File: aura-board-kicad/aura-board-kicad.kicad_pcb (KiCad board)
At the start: 2 copper layers, 76.8 x 53.3 mm, 21 parts, among them J1 Main Power, J2 PWM_3x08, J3 BBCON, J4 Atto, J5 GPS, J6 SBUS, J7 Tele, J8 I2C0, U1 TSR2-2450, U2 PocketBeagle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

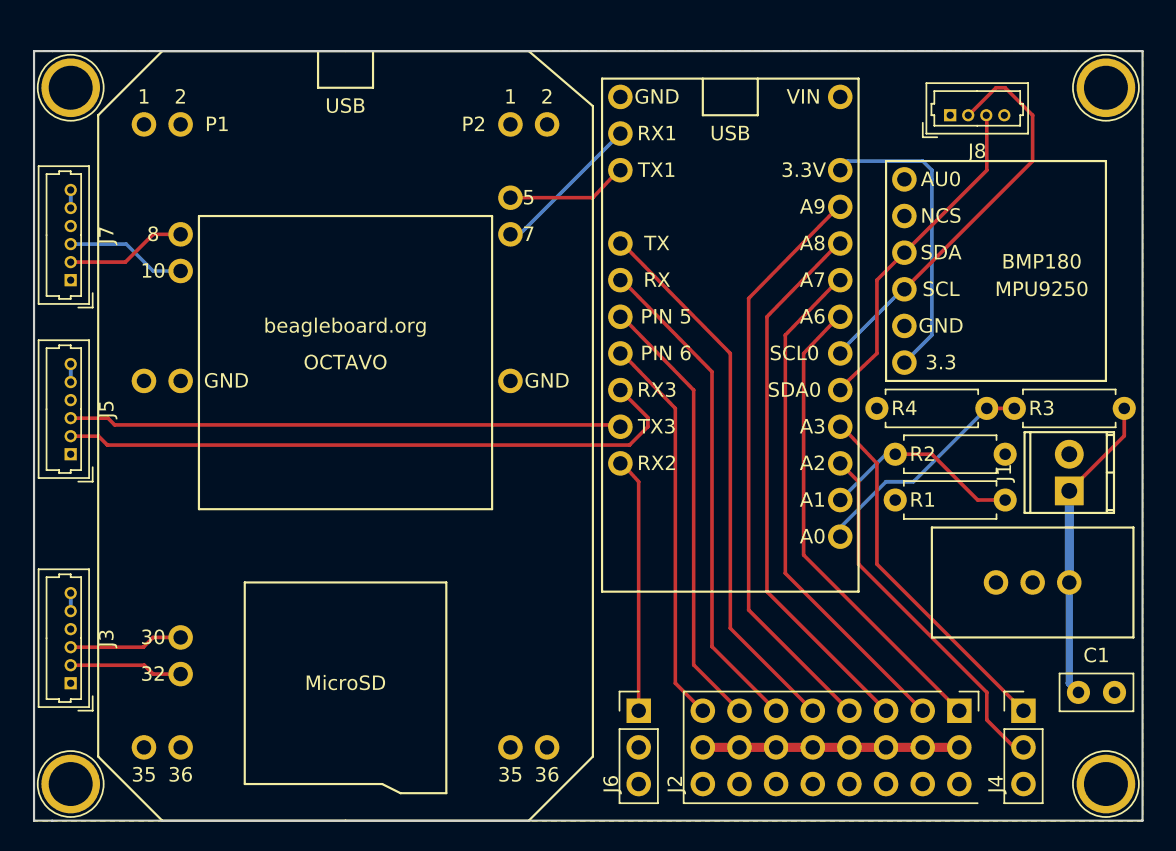
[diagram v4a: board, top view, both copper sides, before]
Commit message: Move some of the F.Fab labels to F.SilkS so they show up on the final board.
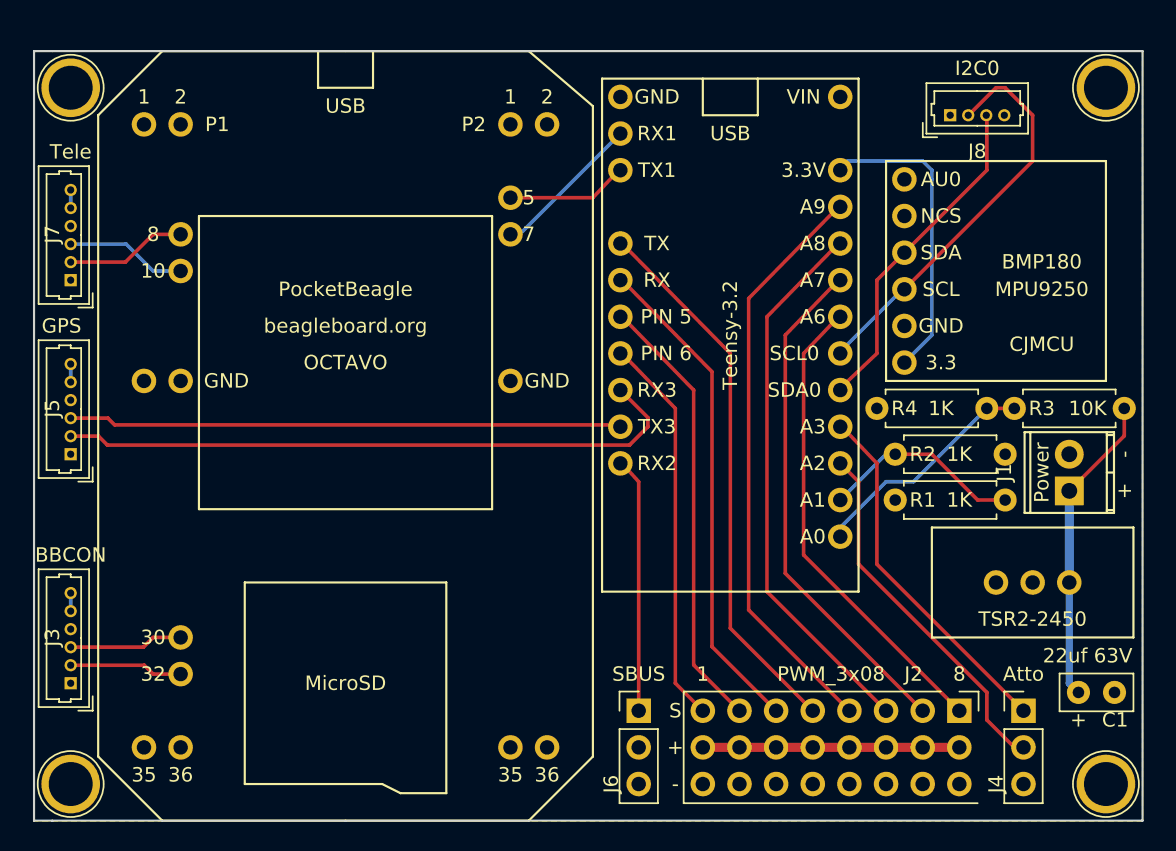
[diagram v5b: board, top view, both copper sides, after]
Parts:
- J1: value Main Power -> Power
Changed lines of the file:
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@@
   (layers
     (0 F.Cu signal hide)
-    (31 B.Cu signal)
+    (31 B.Cu signal hide)
     (32 B.Adhes user)
     (33 F.Adhes user)
@@
   )
   (setup
-    (last_trace_width 0.254)
+    (last_trace_width 0.1524)
     (user_trace_width 0.254)
     (user_trace_width 0.381)
@@
     (visible_elements FFFFFF7F)
     (pcbplotparams
-      (layerselection 0x00030_80000001)
+      (layerselection 0x00020_80000001)
       (usegerberextensions false)
       (excludeedgelayer true)
@@
       (outputformat 1)
       (mirror false)
-      (drillshape 1)
+      (drillshape 0)
       (scaleselection 1)
       (outputdirectory ""))
@@
     (descr "Molex PicoBlade, single row, top entry type, through hole, PN:53047-0610")
     (tags "connector molex picoblade")
-    (fp_text reference J5 (at 3.125 2.5 90) (layer F.SilkS)
-      (effects (font (size 1 1) (thickness 0.15)))
-    )
-    (fp_text value GPS (at 8.89 -0.635 180) (layer F.Fab)
+    (fp_text reference J5 (at 3.175 -1.27 90) (layer F.SilkS)
+      (effects (font (size 1 1) (thickness 0.15)))
+    )
+    (fp_text value GPS (at 8.89 -0.635 180) (layer F.SilkS)
       (effects (font (size 1 1) (thickness 0.15)))
     )
@@
     (fp_line (start -1.9 1.525) (end -1.9 0.525) (layer F.SilkS) (width 0.12))
     (fp_line (start -1.9 1.525) (end -0.9 1.525) (layer F.SilkS) (width 0.12))
-    (fp_text user %R (at 3.125 -1.25 90) (layer F.Fab)
+    (fp_text user %R (at 6.985 2.54 90) (layer F.Fab)
       (effects (font (size 1 1) (thickness 0.15)))
     )
@@
     (descr "Molex PicoBlade, single row, top entry type, through hole, PN:53047-0610")
     (tags "connector molex picoblade")
-    (fp_text reference J3 (at 3.125 2.5 90) (layer F.SilkS)
-      (effects (font (size 1 1) (thickness 0.15)))
-    )
-    (fp_text value BBCON (at 8.89 0 180) (layer F.Fab)
+    (fp_text reference J3 (at 3.175 -1.27 90) (layer F.SilkS)
+      (effects (font (size 1 1) (thickness 0.15)))
+    )
+    (fp_text value BBCON (at 8.89 0 180) (layer F.SilkS)
       (effects (font (size 1 1) (thickness 0.15)))
     )
@@
     (fp_line (start -1.9 1.525) (end -1.9 0.525) (layer F.SilkS) (width 0.12))
     (fp_line (start -1.9 1.525) (end -0.9 1.525) (layer F.SilkS) (width 0.12))
-    (fp_text user %R (at 3.125 -1.25 90) (layer F.Fab)
+    (fp_text user %R (at 6.985 2.54 90) (layer F.Fab)
       (effects (font (size 1 1) (thickness 0.15)))
     )
@@
     (descr "Molex PicoBlade, single row, top entry type, through hole, PN:53047-0610")
     (tags "connector molex picoblade")
-    (fp_text reference J7 (at 3.125 2.5 90) (layer F.SilkS)
-      (effects (font (size 1 1) (thickness 0.15)))
-    )
-    (fp_text value Tele (at 8.89 0 180) (layer F.Fab)
+    (fp_text reference J7 (at 3.175 -1.27 90) (layer F.SilkS)
+      (effects (font (size 1 1) (thickness 0.15)))
+    )
+    (fp_text value Tele (at 8.89 0 180) (layer F.SilkS)
       (effects (font (size 1 1) (thickness 0.15)))
     )
@@
     (fp_line (start -1.9 1.525) (end -1.9 0.525) (layer F.SilkS) (width 0.12))
     (fp_line (start -1.9 1.525) (end -0.9 1.525) (layer F.SilkS) (width 0.12))
-    (fp_text user %R (at 3.125 -1.25 90) (layer F.Fab)
+    (fp_text user %R (at 6.35 2.54 90) (layer F.Fab)
       (effects (font (size 1 1) (thickness 0.15)))
     )
@@
       (effects (font (size 1 1) (thickness 0.15)))
     )
-    (fp_text value I2C0 (at 1.875 -3.25) (layer F.Fab)
+    (fp_text value I2C0 (at 1.875 -3.25) (layer F.SilkS)
       (effects (font (size 1 1) (thickness 0.15)))
     )
@@
     (descr "Through hole straight pin header, 1x08, 2.54mm pitch, single row")
     (tags "Through hole pin header THT 1x08 2.54mm single row")
-    (fp_text reference J2 (at 5.08 19.685 270) (layer F.SilkS)
-      (effects (font (size 1 1) (thickness 0.15)))
-    )
-    (fp_text value PWM_3x08 (at -2.54 8.89 360) (layer F.Fab)
+    (fp_text reference J2 (at -2.54 3.175 360) (layer F.SilkS)
+      (effects (font (size 1 1) (thickness 0.15)))
+    )
+    (fp_text value PWM_3x08 (at -2.54 8.89 360) (layer F.SilkS)
       (effects (font (size 1 1) (thickness 0.15)))
     )
@@
       (effects (font (size 1 1) (thickness 0.15)))
     )
-    (fp_text value 1K (at 3.81 2.31) (layer F.Fab)
+    (fp_text value 1K (at 5.715 3.175) (layer F.SilkS)
       (effects (font (size 1 1) (thickness 0.15)))
     )
@@
       (effects (font (size 1 1) (thickness 0.15)))
     )
-    (fp_text value 10K (at 5.08 0) (layer F.Fab)
+    (fp_text value 10K (at 5.08 0) (layer F.SilkS)
       (effects (font (size 1 1) (thickness 0.15)))
     )
@@
       (effects (font (size 1 1) (thickness 0.15)))
     )
-    (fp_text value 1K (at 4.445 3.175 180) (layer F.Fab)
+    (fp_text value 1K (at 4.445 3.175 180) (layer F.SilkS)
       (effects (font (size 1 1) (thickness 0.15)))
     )
@@
       (effects (font (size 1 1) (thickness 0.15)))
     )
-    (fp_text value 1K (at 3.81 2.31 180) (layer F.Fab)
+    (fp_text value 1K (at 3.175 0 180) (layer F.SilkS)
       (effects (font (size 1 1) (thickness 0.15)))
     )
@@
       (effects (font (size 1 1) (thickness 0.15)))
     )
-    (fp_text value SBUS (at 0 -2.54) (layer F.Fab)
+    (fp_text value SBUS (at 0 -2.54) (layer F.SilkS)
       (effects (font (size 1 1) (thickness 0.15)))
     )
@@
       (effects (font (size 1 1) (thickness 0.15)))
     )
-    (fp_text value Atto (at 0 -2.54) (layer F.Fab)
+    (fp_text value Atto (at 0 -2.54) (layer F.SilkS)
       (effects (font (size 1 1) (thickness 0.15)))
     )
@@
       (effects (font (size 1 1) (thickness 0.15)))
     )
-    (fp_text value "Main Power" (at 1.905 -2.54 90) (layer F.Fab)
+    (fp_text value Power (at 1.27 -1.905 90) (layer F.SilkS)
       (effects (font (size 1 1) (thickness 0.15)))
     )
@@
     (descr "C, Disc series, Radial, pin pitch=2.50mm, , diameter*width=5*2.5mm^2, Capacitor, http://cdn-reichelt.de/documents/datenblatt/B300/DS_KERKO_TC.pdf")
     (tags "C Disc series Radial pin pitch 2.50mm  diameter 5mm width 2.5mm Capacitor")
-    (fp_text reference C1 (at 1.25 -2.56) (layer F.SilkS)
-      (effects (font (size 1 1) (thickness 0.15)))
-    )
-    (fp_text value "22uf 63V" (at 0.635 -2.54) (layer F.Fab)
+    (fp_text reference C1 (at 2.54 1.905) (layer F.SilkS)
+      (effects (font (size 1 1) (thickness 0.15)))
+    )
+    (fp_text value "22uf 63V" (at 0.635 -2.54) (layer F.SilkS)
       (effects (font (size 1 1) (thickness 0.15)))
     )
@@
       (effects (font (size 1 1) (thickness 0.15)))
     )
-    (fp_text value TSR2-2450 (at 0 1.27 180) (layer F.Fab)
+    (fp_text value TSR2-2450 (at 0 1.27 180) (layer F.SilkS)
       (effects (font (size 1 1) (thickness 0.15)))
     )
@@
       (effects (font (size 1 1) (thickness 0.15)))
     )
-    (fp_text value PocketBeagle (at 0 16.51) (layer F.Fab)
+    (fp_text value PocketBeagle (at 0 16.51) (layer F.SilkS)
       (effects (font (size 1 1) (thickness 0.15)))
     )
@@
       (effects (font (size 1 1) (thickness 0.15)))
     )
-    (fp_text value Teensy-3.2 (at 0 17.78 90) (layer F.Fab)
+    (fp_text value Teensy-3.2 (at 0 17.78 90) (layer F.SilkS)
       (effects (font (size 1 1) (thickness 0.15)))
     )
@@
       (effects (font (size 1 1) (thickness 0.15)))
     )
-    (fp_text value CJMCU (at 0 -1.27 180) (layer F.Fab)
+    (fp_text value CJMCU (at -3.175 2.54 180) (layer F.SilkS)
       (effects (font (size 1 1) (thickness 0.15)))
     )
@@
       (net 33 "Net-(U4-Pad6)"))
   )
-  (gr_text + (at 100.33 95.885) (layer F.Fab)
+  (gr_text + (at 100.33 95.885) (layer F.SilkS)
     (effects (font (size 1 1) (thickness 0.25)))
   )
-  (gr_text S (at 72.39 95.25) (layer F.Fab)
+  (gr_text S (at 72.39 95.25) (layer F.SilkS)
     (effects (font (size 1 1) (thickness 0.25)))
   )
-  (gr_text + (at 72.39 97.79) (layer F.Fab)
+  (gr_text + (at 72.39 97.79) (layer F.SilkS)
     (effects (font (size 1 1) (thickness 0.25)))
   )
-  (gr_text - (at 72.39 100.33) (layer F.Fab)
+  (gr_text - (at 72.39 100.33) (layer F.SilkS)
     (effects (font (size 1 1) (thickness 0.25)))
   )
-  (gr_text 8 (at 92.075 92.71) (layer F.Fab)
+  (gr_text 8 (at 92.075 92.71) (layer F.SilkS)
     (effects (font (size 1 1) (thickness 0.25)))
   )
-  (gr_text 1 (at 74.295 92.71) (layer F.Fab)
+  (gr_text 1 (at 74.295 92.71) (layer F.SilkS)
     (effects (font (size 1 1) (thickness 0.25)))
   )
-  (gr_text - (at 103.505 77.47 90) (layer F.Fab)
+  (gr_text - (at 103.505 77.47 90) (layer F.SilkS)
     (effects (font (size 1 1) (thickness 0.25)))
   )
-  (gr_text + (at 103.505 80.01 90) (layer F.Fab)
+  (gr_text + (at 103.505 80.01 90) (layer F.SilkS)
     (effects (font (size 1 1) (thickness 0.25)))
   )
@@
   (segment (start 60.96 59.69) (end 66.675 59.69) (width 0.25) (layer F.Cu) (net 29))
   (segment (start 66.675 59.69) (end 68.58 57.658) (width 0.25) (layer F.Cu) (net 29) (status 20))
-  (segment (start 60.96 62.23) (end 61.595 62.23) (width 0.254) (layer B.Cu) (net 30) (status C00000))
-  (segment (start 61.595 62.23) (end 68.58 55.245) (width 0.254) (layer B.Cu) (net 30) (status C00000))
+  (segment (start 60.96 62.23) (end 61.595 62.23) (width 0.254) (layer B.Cu) (net 30))
+  (segment (start 61.595 62.23) (end 68.58 55.245) (width 0.254) (layer B.Cu) (net 30))
   (segment (start 88.265 71.12) (end 90.17 69.215) (width 0.254) (layer B.Cu) (net 31))
   (segment (start 89.535 57.15) (end 84.328 57.15) (width 0.254) (layer B.Cu) (net 31))
